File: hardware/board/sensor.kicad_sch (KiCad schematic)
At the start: 37 parts, among them J10 Conn_01x03, J11 Conn_01x03, J3 Conn_01x03, J6 Conn_01x03, J7 Conn_01x03, J9 Conn_01x03, Q2 MMBT3904, U10 BMI088, U2 PCA9685PW,118, U4 BMP388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

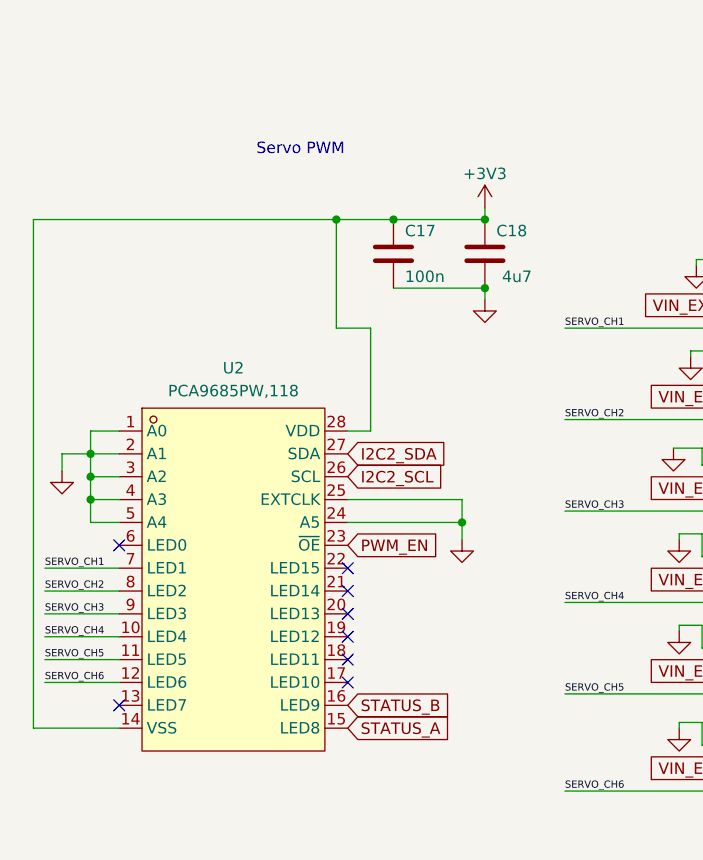
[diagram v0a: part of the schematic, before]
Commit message: #36 Fix short in PCA9865, Remove 'TP' silkscreens
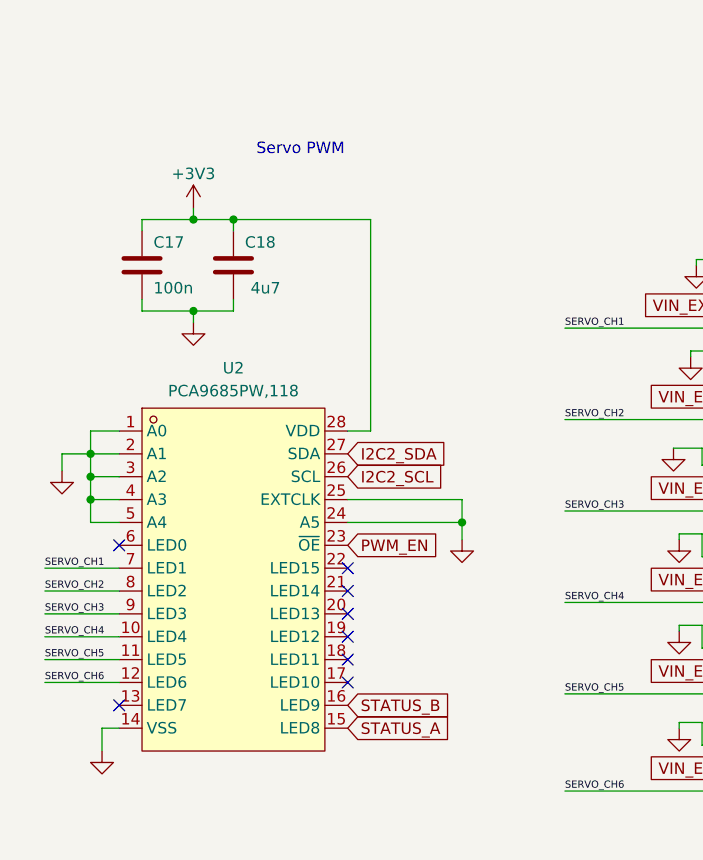
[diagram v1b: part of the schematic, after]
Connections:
- net +3V3: no longer U2.14 (VSS)
- net GND: now also U2.14 (VSS)
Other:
- moved on the sheet: C17, C18

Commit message: Re-organize test points. Fix LED footprints #36
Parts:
- D2: footprint ofc_sym:LED0603-R-RD_WHITE -> LED_SMD:LED_0603_1608Metric
- D2: footprint ofc_sym:LED0603-RD -> LED_SMD:LED_0603_1608Metric
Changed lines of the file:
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@@
       (effects (font (size 1.27 1.27)) (justify right))
     )
-    (property "Footprint" "ofc_sym:LED0603-R-RD_WHITE" (at 142.24 175.26 90)
+    (property "Footprint" "LED_SMD:LED_0603_1608Metric" (at 142.24 175.26 90)
       (effects (font (size 1.27 1.27)) hide)
     )
@@
       (effects (font (size 1.27 1.27)) (justify right))
     )
-    (property "Footprint" "ofc_sym:LED0603-RD" (at 127.635 175.26 90)
-      (effects (font (size 1.27 1.27)) hide)
-    )
+    (property "Footprint" "LED_SMD:LED_0603_1608Metric" (at 127.635 175.26 90)
+      (effects (font (size 1.27 1.27)) hide)
+    )

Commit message: v3 schematic + layout
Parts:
- removed TP19, TP20, TP21, TP22, TP23, TP24: TestPoint, TestPoint:TestPoint_Pad_D1.5mm, symbol Connector:TestPoint
- added C17 (x2): 100n, Capacitor_SMD:C_0402_1005Metric, symbol Device:C
- added D2: KT-0603W, LED_SMD:LED_0603_1608Metric, symbol Device:LED_Small
- added J16, J17: Conn_01x03, Connector_JST:JST_PH_B3B-PH-K_1x03_P2.00mm_Vertical, symbol Connector_Generic:Conn_01x03
- added R1: 5K1, Resistor_SMD:R_0402_1005Metric, symbol Device:R_Small
- added R18: 680, Resistor_SMD:R_0603_1608Metric, symbol Device:R_Small
- added TP1: TestPoint, TestPoint:TestPoint_Pad_D1.5mm, symbol Connector:TestPoint
- added U11: HDC1080, Package_SON:Texas_PWSON-N6, symbol Sensor_Humidity:HDC1080
- added U7: ~, Package_SO:SOIC-16W_7.5x10.3mm_P1.27mm, symbol Sensor_Pressure:SM9541
- renumbered J3 to J10, J6 to J11, J7 to J12, J9 to J13, J10 to J14, J11 to J15
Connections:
- net ACCEL_INT is gone; now on an unnamed net: U10.16 (INT1)
- net +3V3: now also C17.1, C17.2, R1.1, U11.5 (VCC), U7.7 (VDD); no longer U10.14 (CSB1), U10.7 (PS), U4.6 (CSB), U5.10 (CS)
- net GND: now also U10.7 (PS), C17.1, C17.2, D2.1 (K), J16.1 (Pin_1), J17.1 (Pin_1), U11.2 (GND), U7.6 (VSS); no longer U10.10 (SDO2), U10.15 (SDO1), U4.5 (SDO), U5.9 (SD0/SA1)
- net I2C1_SCL: now also U2.26 (SCL); no longer U10.8 (SCL/SCK), U4.2 (SCK), U5.1 (SCL/SPC)
- net I2C1_SDA: now also U2.27 (SDA); no longer U10.9 (SDA/SDI), U4.4 (SDI), U5.11 (SDA/SDI/SDO)
- net I2C2_SCL: no longer U2.26 (SCL)
- net I2C2_SDA: no longer U2.27 (SDA)
- net VIN_EXT: now also J16.2 (Pin_2), J17.2 (Pin_2)
- net SERVO_CH7: now reaches U2.17 (LED10)
- net SERVO_CH7: now also J16.3 (Pin_3)
- net SERVO_CH8: now reaches U2.18 (LED11)
- net SERVO_CH8: now also J17.3 (Pin_3)
- net STATUS_C: now reaches U2.19 (LED12)
- net STATUS_C: now also R18.1
- net VBZ: now reaches BZ1.N (+), Q2.3 (C)
- net VBZ: now also TP1.1
- net IMU_DRDY: now reaches U10.1 (INT2)
- net GYR_CS: now reaches U10.5 (CSB2)
- net GNSS_SAFEBOOT: no longer names the net of U8.1 (~{SAFEBOOT})
- net GYRO_INT: no longer names the net of U10.13 (INT4)
- net PRES_INT renamed PRES_DRDY
- new net: D2.2 (A), R18.2
- new net ACC_CS: U10.14 (CSB1)
- new net I2C3_ SCL: U11.6 (SCL), U7.11 (SCL)
- new net I2C3_SDA: U11.1 (SDA), U7.10 (SDA)
- new net MAG_CS: R1.2, U5.10 (CS)
- new net PRES_CS: U4.6 (CSB)
- new net SPI3_MISO: U10.10 (SDO2), U10.15 (SDO1), U4.5 (SDO), U5.9 (SD0/SA1)
- new net SPI3_MOSI: U10.9 (SDA/SDI), U4.4 (SDI), U5.11 (SDA/SDI/SDO)
- new net SPI3_SCK: U10.8 (SCL/SCK), U4.2 (SCK), U5.1 (SCL/SPC)
- no-connect marks 18 -> 13
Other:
- note added: "Airspeed Diff. Pressure"
- note added: "Humidity + Temp"
- moved on the sheet: BZ1, C14, C15, C26, J10, J11, J12, J13, J14, J15, JP1, L1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

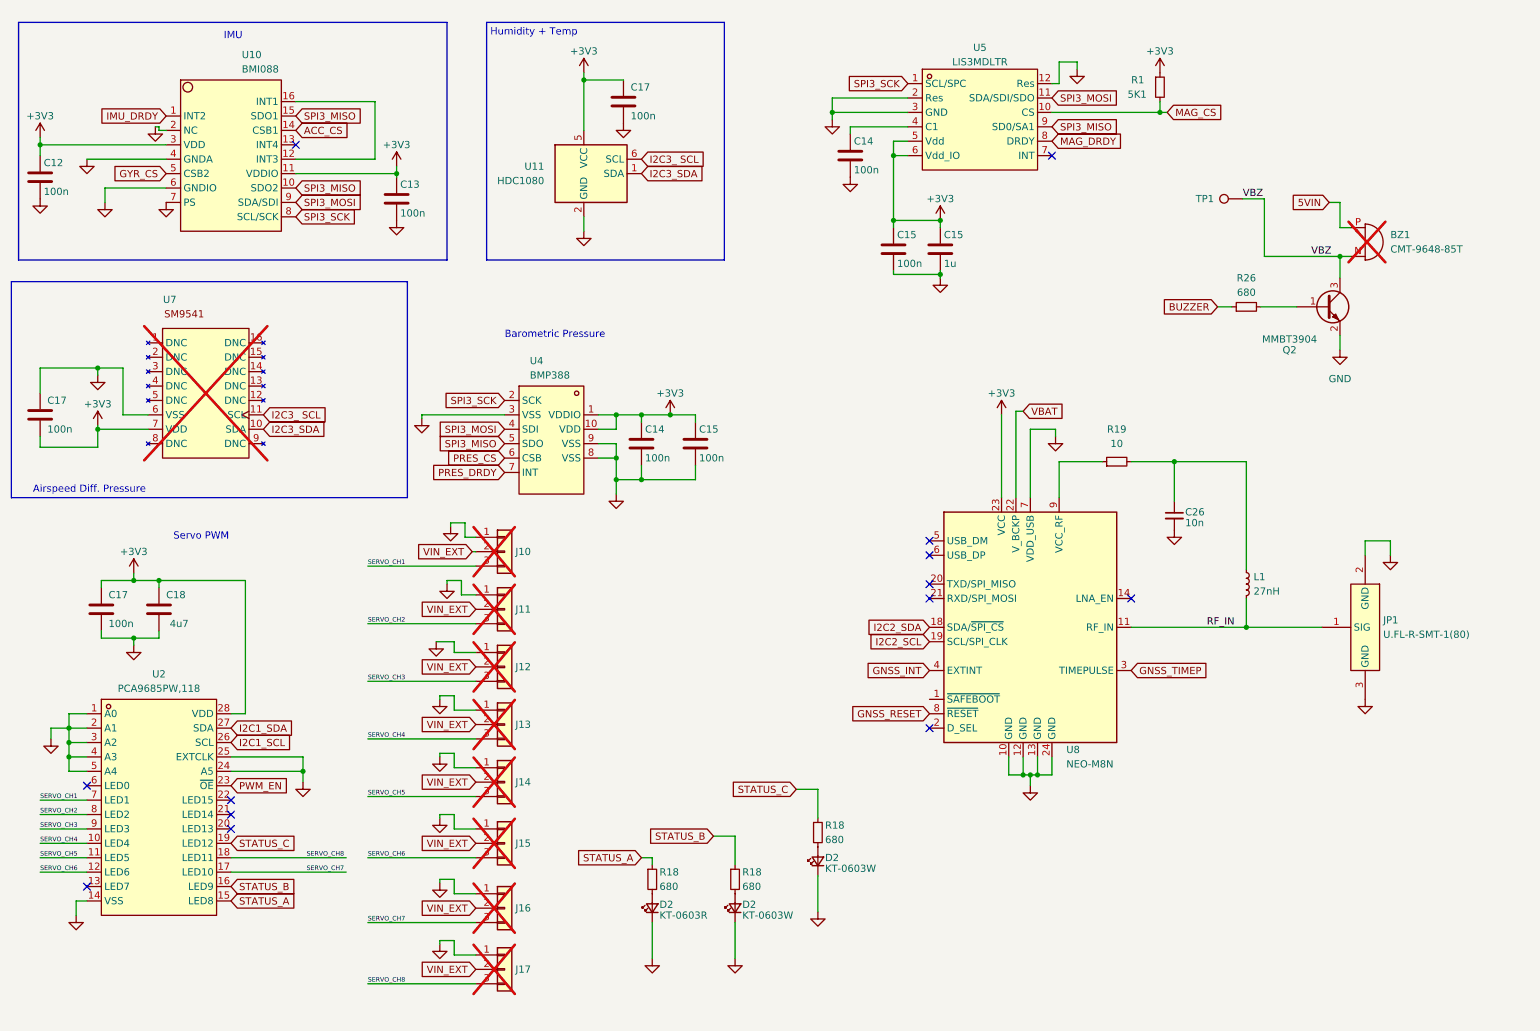
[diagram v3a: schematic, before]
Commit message: Added some organization to schematic
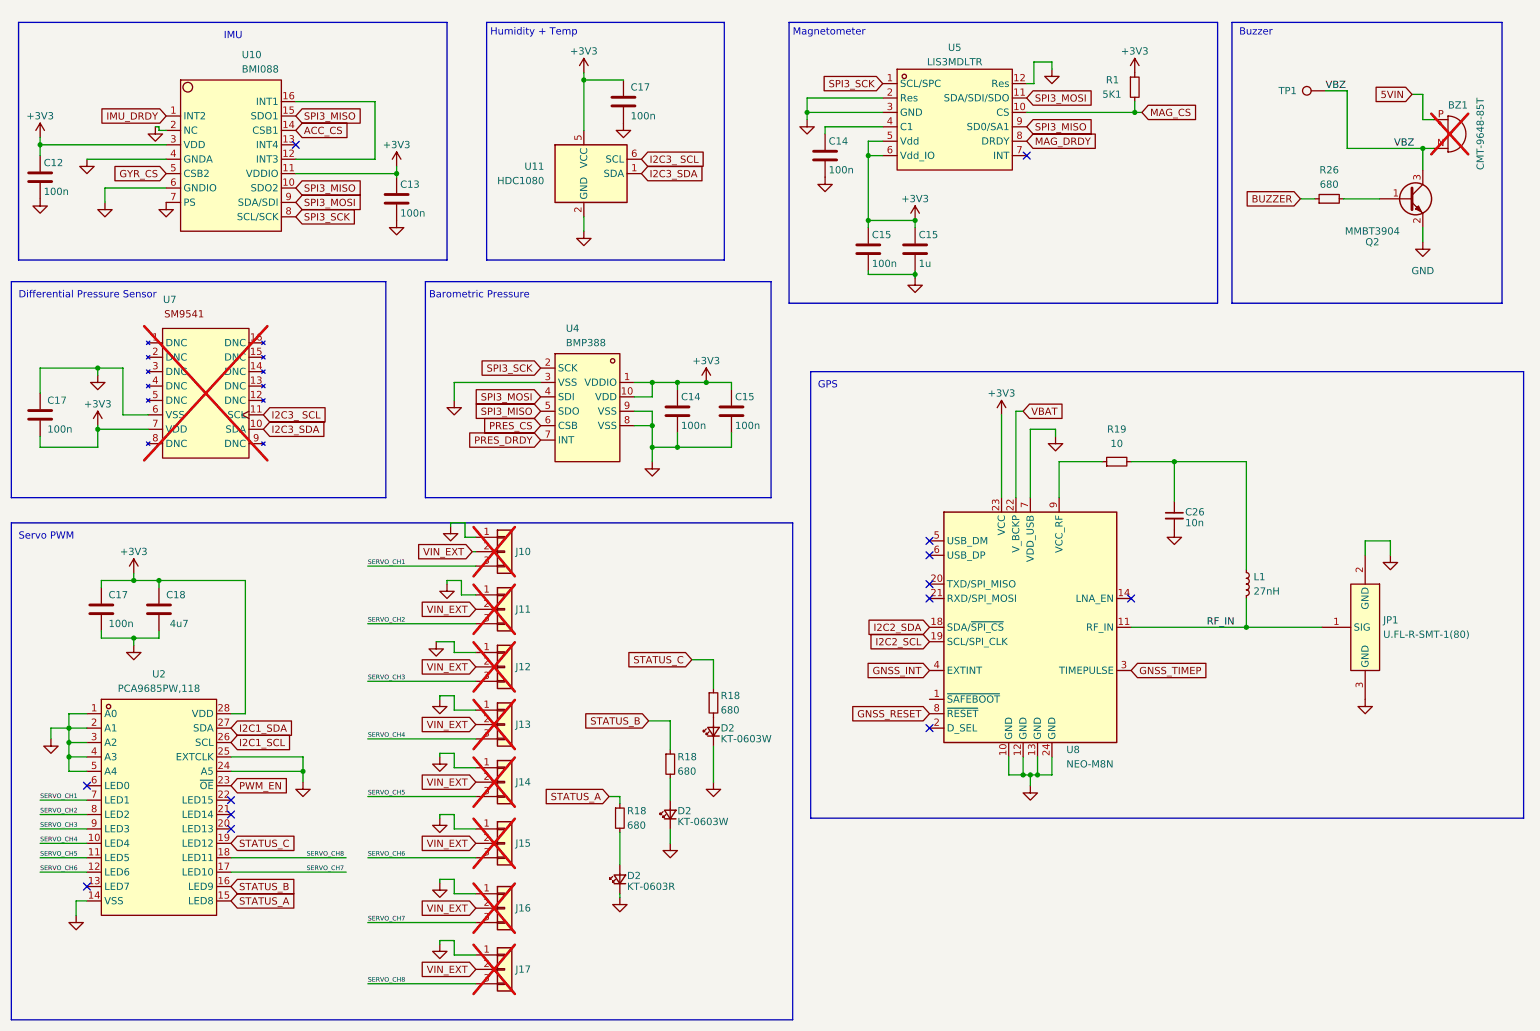
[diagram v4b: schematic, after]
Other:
- note added: "Buzzer"
- note added: "Differential Pressure Sensor"
- note added: "GPS"
- note added: "Magnetometer"
- note removed: "Airspeed Diff. Pressure"
- moved on the sheet: BZ1, C14, C15, D2, Q2, R1, R18, R26, TP1, U4, U5

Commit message: dead-end board files
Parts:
- added C15: 100n, Capacitor_SMD:C_0402_1005Metric, symbol Device:C
- added C15: 1u, Capacitor_SMD:C_0402_1005Metric, symbol Device:C
- added R1 (x4): 5K1, Resistor_SMD:R_0402_1005Metric, symbol Device:R_Small
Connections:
- net +3V3: now also R1.1, R1.1, R1.1, R1.1; no longer R1.1
- net 5VIN: now also C15.1, C15.1
- net ACC_CS: now also R1.2
- net GND: now also R1.1, C15.2, C15.2; no longer U2.1 (A0)
- net GYR_CS: now also R1.2
- net PRES_CS: now also R1.2
- new net: R1.2, U2.1 (A0)
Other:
- moved on the sheet: C12, C13, C17, C26, L1, R1, R19, TP1, U10, U11, U8
